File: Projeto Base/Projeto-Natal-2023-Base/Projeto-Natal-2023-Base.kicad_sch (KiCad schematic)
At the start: 40 parts, among them U1 STM8S003F3P

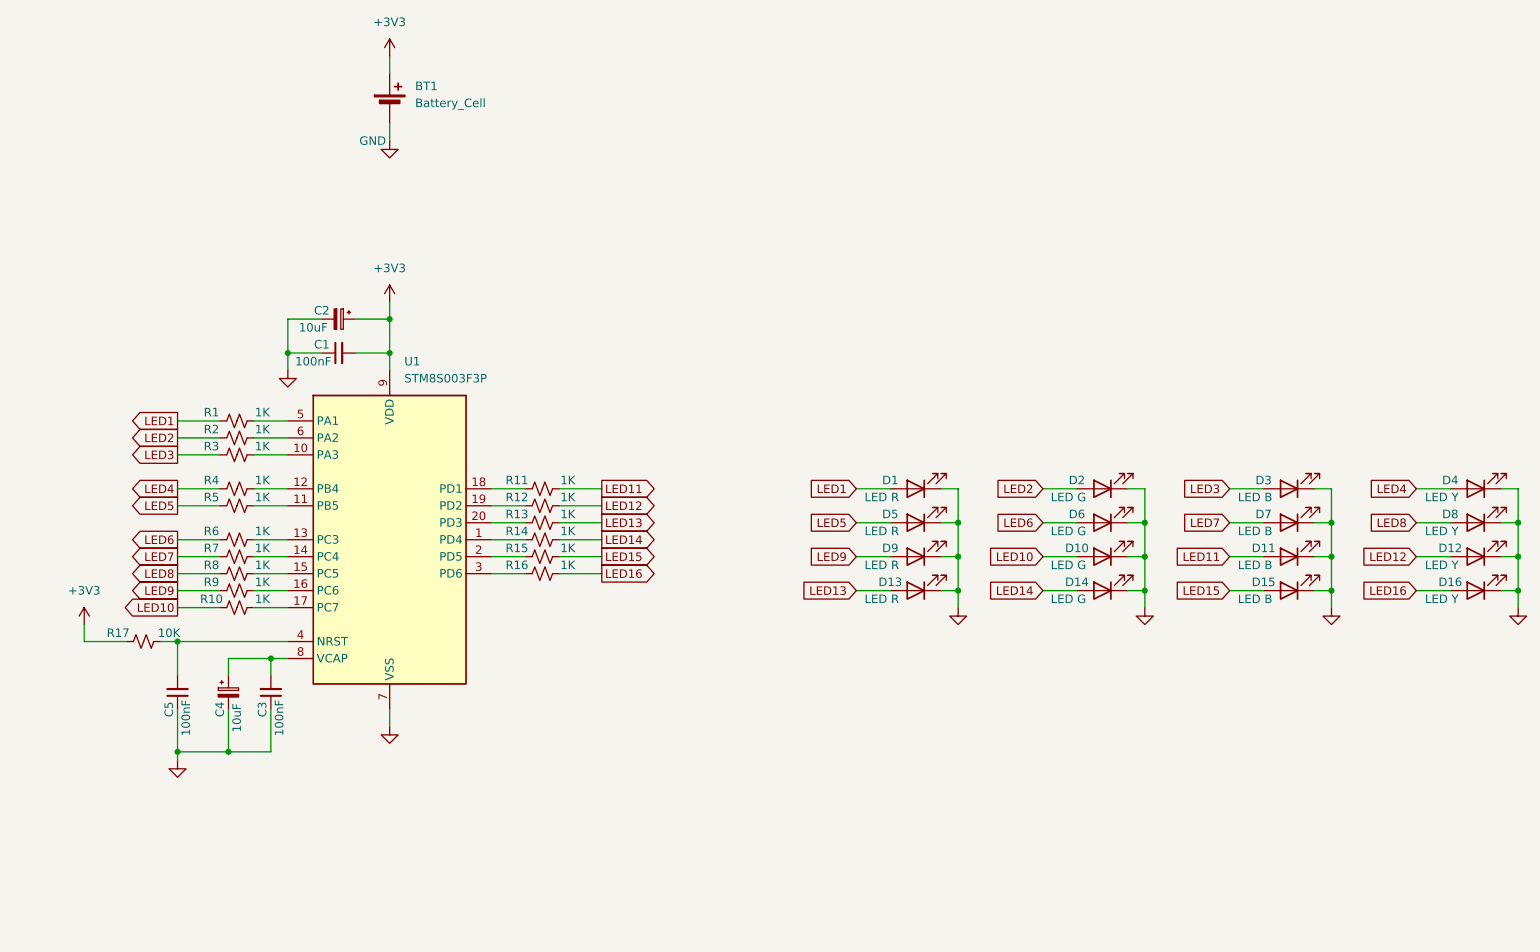
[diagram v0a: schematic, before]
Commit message: trocando mcu para ch32v003f4p6
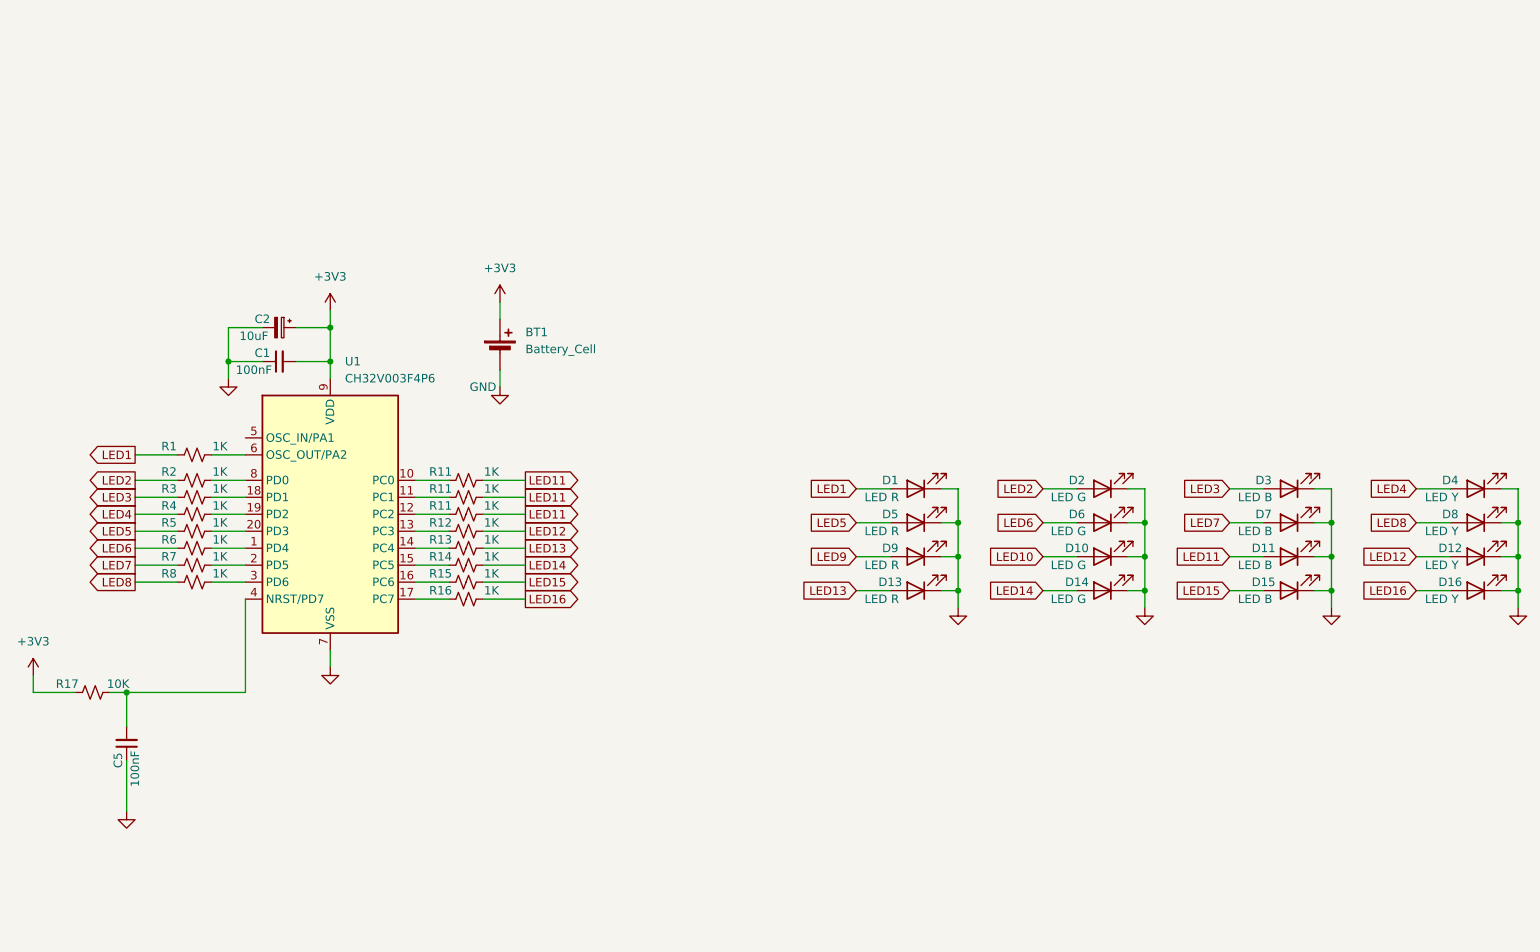
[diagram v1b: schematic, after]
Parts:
- removed C3: 100nF, Capacitor_SMD:C_0603_1608Metric_Pad1.08x0.95mm_HandSolder, symbol Device:C_Small
- removed C4: 10uF, Capacitor_SMD:C_0805_2012Metric_Pad1.18x1.45mm_HandSolder, symbol Device:C_Polarized_Small
- removed R10, R9: 1K, Resistor_SMD:R_0603_1608Metric_Pad0.98x0.95mm_HandSolder, symbol Device:R_Small_US
- removed U1: STM8S003F3P, Package_SO:TSSOP-20_4.4x6.5mm_P0.65mm, symbol MCU_ST_STM8:STM8S003F3P
- added R11 (x2): 1K, Resistor_SMD:R_0603_1608Metric_Pad0.98x0.95mm_HandSolder, symbol Device:R_Small_US
- added U1: CH32V003F4P6, Package_SO:TSSOP-20_4.4x6.5mm_P0.65mm, symbol wch_mcu:CH32V003F4P6
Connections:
- net +3V3: now also U1.9 (VDD)
- net GND: now also U1.7 (VSS)
- net LED11: now also R11.2, R11.2
- net at R13.1: now also U1.14 (PC4)
- net at R11.1: now also U1.12 (PC2)
- net at R2.2: now also U1.8 (PD0)
- net at R1.2: now also U1.6 (OSC_OUT/PA2)
- net at R14.1: now also U1.15 (PC5)
- net at R4.2: now also U1.19 (PD2)
- net at R7.2: now also U1.2 (PD5)
- net at R5.2: now also U1.20 (PD3)
- net at R12.1: now also U1.13 (PC3)
- net at C5.2, R17.2: now also U1.4 (NRST/PD7)
- net at R3.2: now also U1.18 (PD1)
- net at R6.2: now also U1.1 (PD4)
- net at R8.2: now also U1.3 (PD6)
- net at R15.1: now also U1.16 (PC6)
- net at R16.1: now also U1.17 (PC7)
- new net: R11.1, U1.10 (PC0)
- new net: R11.1, U1.11 (PC1)
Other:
- moved on the sheet: BT1, C5, R1, R11, R12, R13, R14, R15, R16, R17, R2, R3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

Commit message: Adicionando conector de SWIO
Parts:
- added J1: Conn_01x03_Pin, Connector_PinHeader_2.54mm:PinHeader_1x03_P2.54mm_Vertical, symbol Connector:Conn_01x03_Pin
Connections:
- net +3V3: now also J1.1 (Pin_1)
- net GND: now also J1.2 (Pin_2)
- net at R2.2: now also U1.6 (OSC_OUT/PA2); no longer U1.8 (PD0)
- net at R1.2: now also U1.5 (OSC_IN/PA1); no longer U1.6 (OSC_OUT/PA2)
- net at R3.2: now also U1.8 (PD0); no longer U1.18 (PD1)
- new net SWIO: J1.3 (Pin_3), U1.18 (PD1)
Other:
- moved on the sheet: R1, R2, R3
